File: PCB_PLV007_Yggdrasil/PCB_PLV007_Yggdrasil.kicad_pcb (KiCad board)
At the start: 2 copper layers, 75 x 100 mm, 114 parts, among them J1 Conn_01x12, J2 UMBILICAL_MASTER, J3 UMBILICAL_POWER, Q1 DMG2302UK-7, Q2 DMP2123L-7, Q3 MMBTA06LT1G, Q4 DMG2302UK-7, Q5 DMP2123L-7, U1 R-78C12-1.0, U10 LM2902, U11 BTS50055-1TMA, U2 BME280, U3 SN65HVD232, U4 74HC21, U5 74HC266, U6 74HC08, U7 74HC21, U8 74LVC1G17, U9 LTC6993xS6-1

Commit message: Idek anymore
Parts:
- added G***: LOGO, BoringFootprints:Paradigm_NameBelow_12.7mm, F.Cu at (76.8, 130.8)
- added REF**: Paradigm_Title_Block, BoringFootprints:Paradigm_Title_Block, F.Cu at (63.0, 143.2)
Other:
- board text added: "A"
- board text added: "PLV007_Yggdrasil"
- board text added: "Paradigm Boring"
- board text added: "Yggdrasil Surface Interface Board"

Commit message: Updated Yggdrasil layout/routing (first draft)
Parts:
- C11, C14, C15, C16, C17, C19, C20, C23, C24, D11, D6, D7, D8, D9, JP2, Q1, Q2, R11, R13, R17, R27, R29, R30, R31, R32, R33, R41, R43, R47, R50, R51, U3, U8, U9: moved to B.Cu
- C22, F2, Q3, R28, R34, R35, R36, R37, R38, R39, R40, R42, R46, U10, U11: moved to F.Cu
- moved D8 74.9 mm to (114.4, 59.3), turned to 270 degrees
- moved R41 74.9 mm to (116.7, 59.3), turned to 270 degrees
- moved R42 74.9 mm to (111.7, 59.3), turned to 270 degrees
- moved Q3 73.9 mm to (108.7, 59.8), turned to 270 degrees
- moved R46 66.5 mm to (109.6, 63.6), turned to 180 degrees
- moved C18 65.1 mm to (98.2, 131.0), turned to 90 degrees
- moved U11 61.5 mm to (98.2, 66.4), turned to 270 degrees
- moved C22 57.7 mm to (112.8, 65.4), turned to 0 degrees
- moved D9 57.1 mm to (117.2, 70.1)
- moved C23 55.6 mm to (115.2, 70.1)
- moved R47 55.3 mm to (121.3, 70.2), turned to 270 degrees
- moved D11 54.8 mm to (123.2, 70.2), turned to 90 degrees
- moved R43 54.4 mm to (112.6, 70.1)
- moved C24 54.3 mm to (119.5, 70.2), turned to 90 degrees
- moved U10 54.0 mm to (112.2, 70.1), turned to 270 degrees
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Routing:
- net /UHBLS/UMBILICAL_V+: track 14.6 -> 160.3 mm, vias 1 -> 2
- net GND: track 65.1 -> 195.7 mm, vias 61 -> 38
- net /LOAD_SWITCH: track 54.9 -> 125.2 mm
- net /UHB: track 114.0 -> 58.8 mm, vias 4 -> 1
- net /C_SAFE: track 49.3 -> 101.4 mm, vias 0 -> 1
- net /HEARTBEAT_ADDRESS_3: track 75.1 -> 123.2 mm, vias 2 -> 1
- net +3V3: track 196.1 -> 237.2 mm, vias 9 -> 4
- net /HEARTBEAT_ADDRESS_4: track 62.3 -> 101.9 mm, vias 2 -> 1
- net Net-(D6-Pad2): track 54.9 -> 17.4 mm, vias 1 -> 0
- net /HEARTBEAT_ADDRESS_2: track 91.4 -> 128.9 mm, vias 3 -> 2
- net /V_SAFE: track 66.5 -> 103.2 mm
- net Net-(R19-Pad2): track 2.00 -> 31.1 mm
- net /UHBLS/UHB_MASTER: track 66.8 -> 39.5 mm, vias 2 -> 0
- net /MCU_UHB_INPUT: track 45.6 -> 18.3 mm
- net /V_SENSE: track 30.3 -> 53.2 mm
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- removed copper zone on B.Cu, net +28V
- removed copper zone on B.Cu, net /UHBLS/UMBILICAL_V+
- removed copper zone on B.Cu, net GND

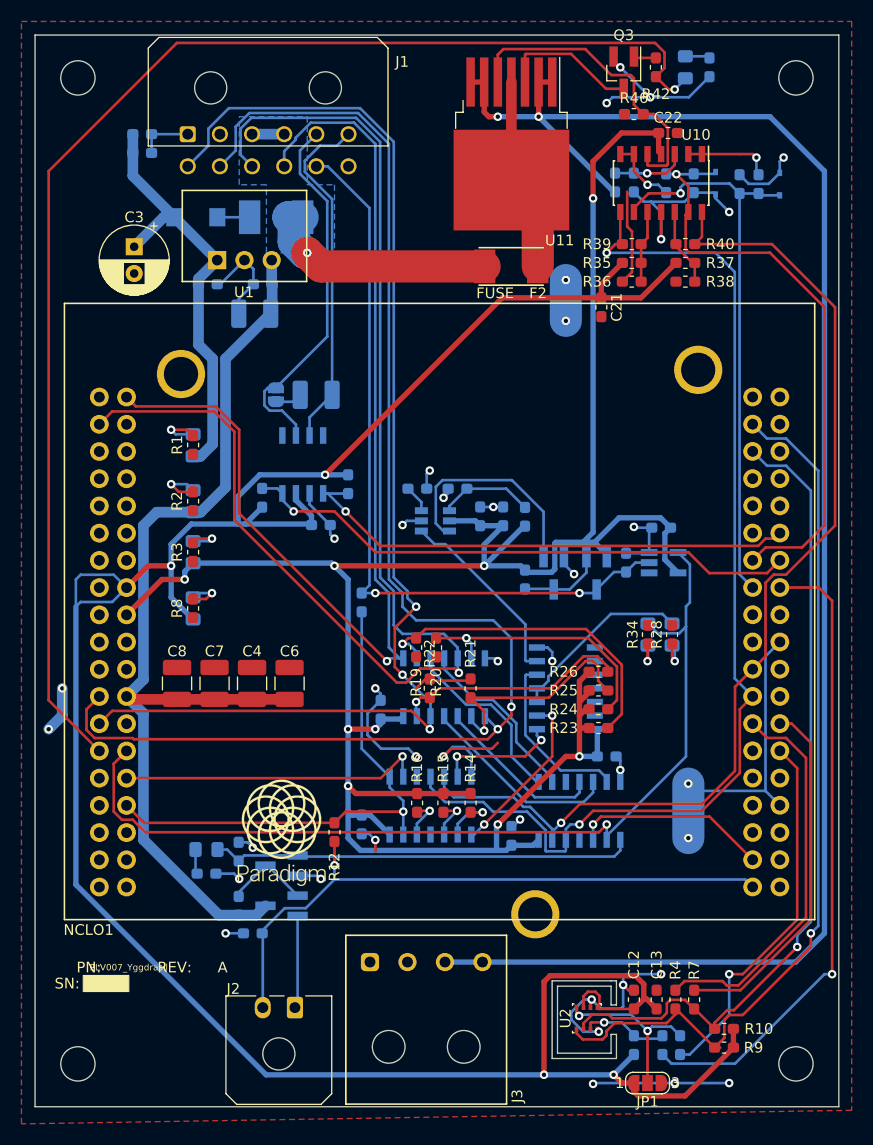
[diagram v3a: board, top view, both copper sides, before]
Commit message: Implementing feedback from Jasper (p.1)
- Trace between F1 and D1 changed to 1.000mm
- Moved Umbilical_V+ to left edge of board, changed trace width to 2.5mm. 1mm trace still used between pads on U11 and from U11 to R50.
- Moved the 3.3V trace that supplies the components on the bottom right corner
- Moved some of the traces on the right side. Long-running overlap should be minimized here now.
- Added a ground plane to the back and cleaned up some of the random traces that I had before. I added keep-outs to get rid of weird or floating fills, and I threw vias in some places to connect the planes when necessary. Likely possible to clean this up a bit more.
- Silkscreen update not started, to come in next commit
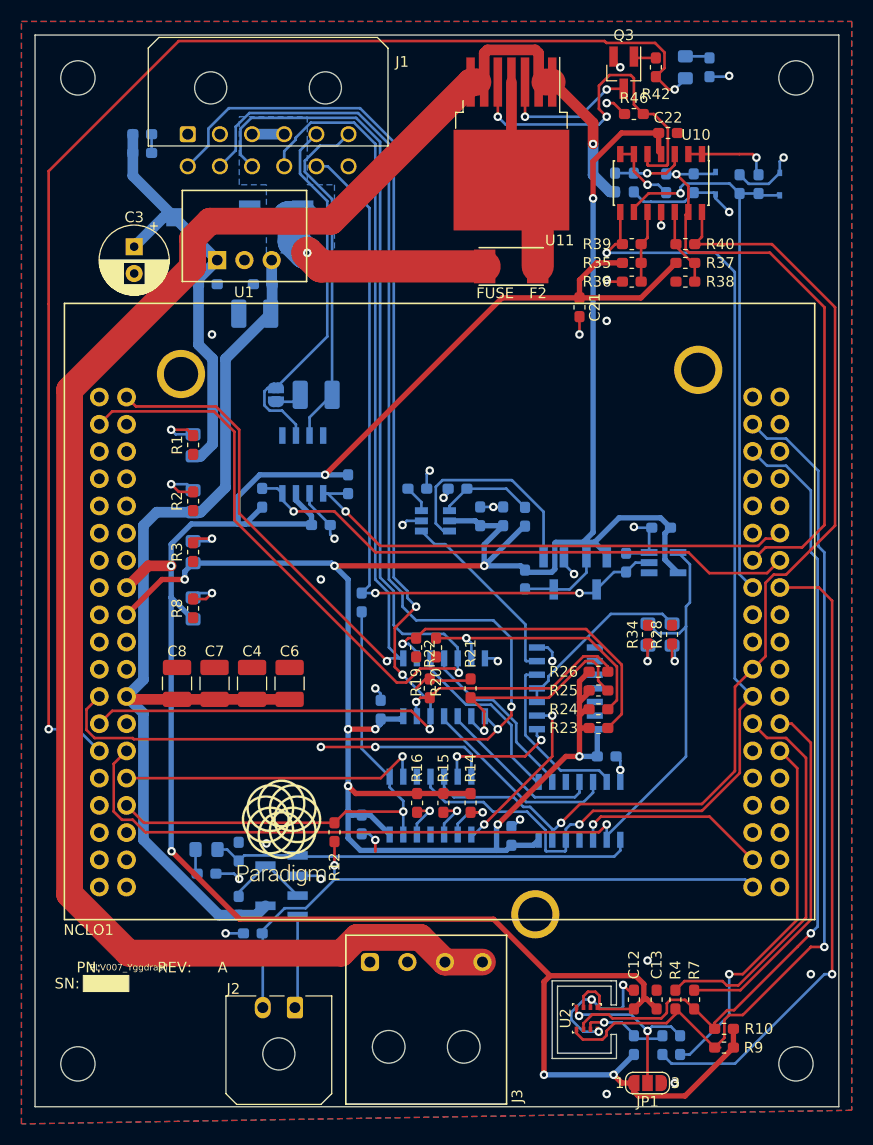
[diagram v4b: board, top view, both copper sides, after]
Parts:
- moved C21 2.04 mm to (104.5, 81.7)
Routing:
- net GND: track 195.7 -> 102.4 mm, vias 38 -> 37
- net +3V3: track 237.2 -> 212.9 mm, vias 4 -> 5
- net /UHBLS/UMBILICAL_V+: track 160.3 -> 165.5 mm, vias 2 -> 1
- net Net-(R46-Pad1): track 29.5 -> 33.9 mm, vias 0 -> 2
- net /LOAD_SWITCH: track 125.2 -> 126.9 mm, vias 1 -> 2
- net /I2C_SCL: track 83.7 -> 84.9 mm
- net /I2C_SDA: track 77.1 -> 77.6 mm
- net Net-(Q3-Pad3): track 13.1 -> 13.5 mm, vias 0 -> 2
- added copper zone on B.Cu, net GND

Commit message: Silkscreen First Pass
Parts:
- moved G*** 22.0 mm to (66.5, 150.2)

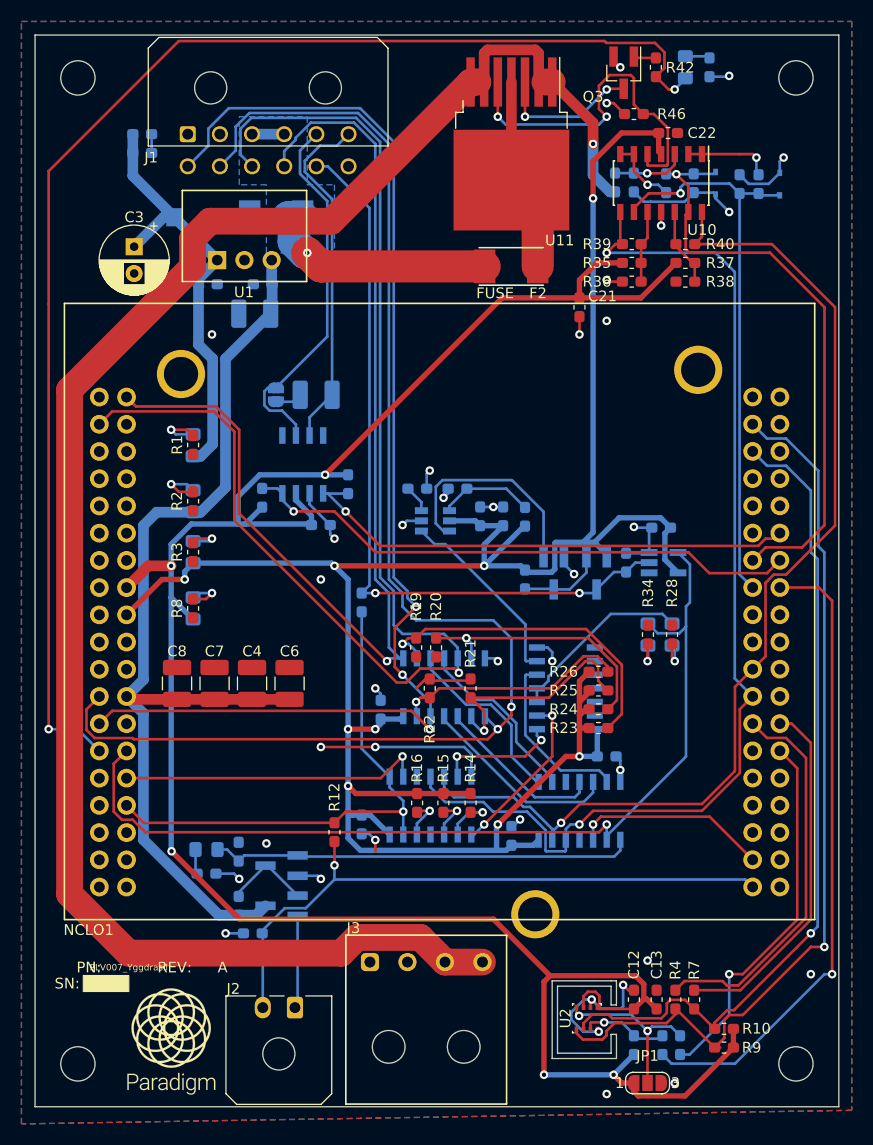
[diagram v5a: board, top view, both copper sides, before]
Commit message: Yggdrasil Minor Routing Fixes
Just cleaned up some unequal trace spacing in places
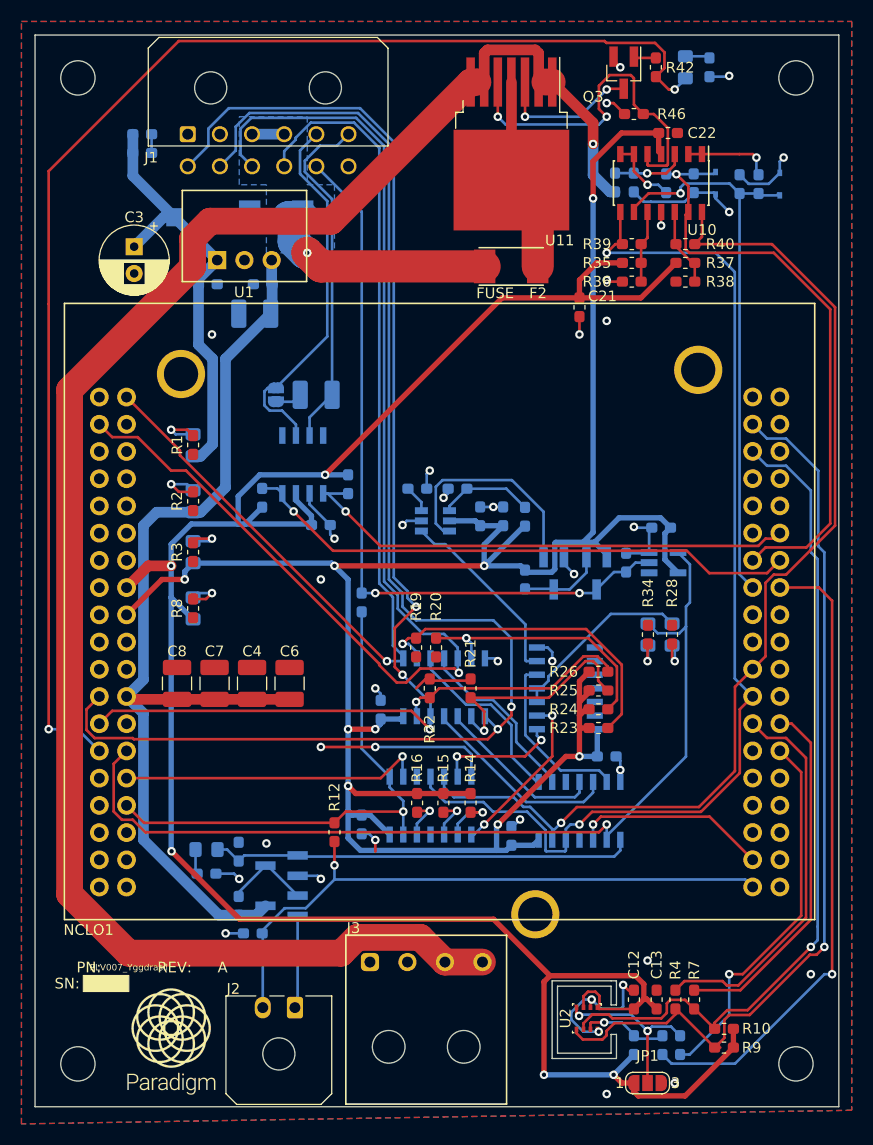
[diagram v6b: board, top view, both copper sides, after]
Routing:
- net /HEARTBEAT_ADDRESS_3: track 123.2 -> 116.4 mm
- net /HEARTBEAT_ADDRESS_4: track 101.9 -> 97.4 mm
- net /HEARTBEAT: track 70.8 -> 69.6 mm
- net /C_SENSE: track 55.9 -> 56.7 mm
- net /I2C_SDA: track 77.6 -> 78.3 mm
